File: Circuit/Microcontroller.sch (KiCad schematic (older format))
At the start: 5 parts, among them CON501 AVR-ISP-10, IC501 ATMEGA644-A, Y501 Crystal

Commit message: Additional PCB work
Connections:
- net ADC0: now also IC501.34 ((PCINT3/ADC3)PA3); no longer IC501.37 ((PCINT0/ADC0)PA0)
- net ADC1: now also IC501.35 ((PCINT2/ADC2)PA2); no longer IC501.36 ((PCINT1/ADC1)PA1)
- net ADC2: now also IC501.36 ((PCINT1/ADC1)PA1); no longer IC501.35 ((PCINT2/ADC2)PA2)
- net ADC3: now also IC501.37 ((PCINT0/ADC0)PA0); no longer IC501.34 ((PCINT3/ADC3)PA3)
- net RST: now also IC501.44 ((PCINT12/OC0B/~SS~)PB4)
- net PD1: now reaches IC501.10 ((PCINT25/TXD0)PD1)
- net PD2: now reaches IC501.11 ((PCINT26/INT0)PD2)
- net PD3: now reaches IC501.12 ((PCINT27/INT1)PD3)
- net PD4: now reaches IC501.13 ((PCINT28/OC1B)PD4)
- net PD5: now reaches IC501.14 ((PCINT294/OC1A)PD5)
- net PD6: now reaches IC501.15 ((PCINT30/OC2B/ICP)PD6)
- net PD7: now reaches IC501.16 ((PCINT31/OC2A)PD7)
- net PC0: now reaches IC501.19 ((PCINT16/SCL)PC0)
- net PC1: now reaches IC501.20 ((PCINT17/SDA)PC1)
- net PC2: now reaches IC501.21 ((PCINT18/TCK)PC2)
- net PC3: now reaches IC501.22 ((PCINT19/TMS)PC3)
- net PC4: now reaches IC501.23 ((PCINT20/TDO)PC4)
- net PC5: now reaches IC501.24 ((PCINT21/TDI)PC5)
- net PC6: now reaches IC501.25 ((PCINT22/TOSC1)PC6)
- net PC7: now reaches IC501.26 ((PCINT23/TOSC2)PC7)
- net WR: now reaches IC501.42 ((PCINT10/AIN0/INT2)PB2)
- net CS: now reaches IC501.43 ((PCINT11/AIN1/OC0A)PB3)
- net PD0: now reaches IC501.9 ((PCINT24/RXD0)PD0)
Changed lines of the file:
@@
 $EndComp
 $Comp
-L GND #PWR048
+L GND #PWR503
 U 1 1 58AFDD43
 P 5150 5750
-F 0 "#PWR048" H 5150 5500 50  0001 C CNN
+F 0 "#PWR503" H 5150 5500 50  0001 C CNN
 F 1 "GND" H 5150 5600 50  0000 C CNN
 F 2 "" H 5150 5750 50  0000 C CNN
@@
 $EndComp
 $Comp
-L GND #PWR049
+L GND #PWR504
 U 1 1 58AFDD54
 P 5350 5750
-F 0 "#PWR049" H 5350 5500 50  0001 C CNN
+F 0 "#PWR504" H 5350 5500 50  0001 C CNN
 F 1 "GND" H 5350 5600 50  0000 C CNN
 F 2 "" H 5350 5750 50  0000 C CNN
@@
 $EndComp
 $Comp
-L GND #PWR050
+L GND #PWR506
 U 1 1 58AFDD65
 P 5550 5750
-F 0 "#PWR050" H 5550 5500 50  0001 C CNN
+F 0 "#PWR506" H 5550 5500 50  0001 C CNN
 F 1 "GND" H 5550 5600 50  0000 C CNN
 F 2 "" H 5550 5750 50  0000 C CNN
@@
 $EndComp
 $Comp
-L GND #PWR051
+L GND #PWR507
 U 1 1 58AFDD76
 P 5750 5750
-F 0 "#PWR051" H 5750 5500 50  0001 C CNN
+F 0 "#PWR507" H 5750 5500 50  0001 C CNN
 F 1 "GND" H 5750 5600 50  0000 C CNN
 F 2 "" H 5750 5750 50  0000 C CNN
@@
 	5600 5700 5600 5650
 $Comp
-L +3.3V #PWR052
+L +3.3V #PWR505
 U 1 1 58AFDE0F
 P 5400 1500
-F 0 "#PWR052" H 5400 1350 50  0001 C CNN
+F 0 "#PWR505" H 5400 1350 50  0001 C CNN
 F 1 "+3.3V" H 5400 1640 50  0000 C CNN
 F 2 "" H 5400 1500 50  0000 C CNN
@@
 RST
 $Comp
-L +3.3V #PWR053
+L +3.3V #PWR508
 U 1 1 58AFE137
 P 10800 900
-F 0 "#PWR053" H 10800 750 50  0001 C CNN
+F 0 "#PWR508" H 10800 750 50  0001 C CNN
 F 1 "+3.3V" H 10800 1040 50  0000 C CNN
 F 2 "" H 10800 900 50  0000 C CNN
@@
 	10800 1150 10800 900
 $Comp
-L GND #PWR054
+L GND #PWR509
 U 1 1 58AFE166
 P 10800 1700
-F 0 "#PWR054" H 10800 1450 50  0001 C CNN
+F 0 "#PWR509" H 10800 1450 50  0001 C CNN
 F 1 "GND" H 10800 1550 50  0000 C CNN
 F 2 "" H 10800 1700 50  0000 C CNN
@@
 $EndComp
 $Comp
-L GND #PWR055
+L GND #PWR501
 U 1 1 58AFE6AE
 P 3350 2350
-F 0 "#PWR055" H 3350 2100 50  0001 C CNN
+F 0 "#PWR501" H 3350 2100 50  0001 C CNN
 F 1 "GND" H 3350 2200 50  0000 C CNN
 F 2 "" H 3350 2350 50  0000 C CNN
@@
 $EndComp
 $Comp
-L GND #PWR056
+L GND #PWR502
 U 1 1 58AFE704
 P 3350 2750
-F 0 "#PWR056" H 3350 2500 50  0001 C CNN
+F 0 "#PWR502" H 3350 2500 50  0001 C CNN
 F 1 "GND" H 3350 2600 50  0000 C CNN
 F 2 "" H 3350 2750 50  0000 C CNN
@@
 Text HLabel 7000 3550 2    60   Input ~ 0
 SCK
+Text HLabel 7000 2250 2    60   Input ~ 0
+ADC0
+Text HLabel 7000 2150 2    60   Input ~ 0
+ADC1
+Text HLabel 7000 2050 2    60   Input ~ 0
+ADC2
 Text HLabel 7000 1950 2    60   Input ~ 0
-ADC0
-Text HLabel 7000 2050 2    60   Input ~ 0
-ADC1
-Text HLabel 7000 2150 2    60   Input ~ 0
-ADC2
-Text HLabel 7000 2250 2    60   Input ~ 0
 ADC3
 Wire Wire Line
@@
 Wire Wire Line
 	6600 2250 7000 2250
+Wire Wire Line
+	6600 3250 7000 3250
+Wire Wire Line
+	6600 3150 7000 3150
+Wire Wire Line
+	6600 3050 7000 3050
+Text Label 6750 3250 0    60   ~ 0
+RST
+Text Label 6800 3150 0    60   ~ 0
+CS
+Text Label 6800 3050 0    60   ~ 0
+WR
+Text HLabel 7000 3250 2    60   Input ~ 0
+RST
+Text HLabel 7000 3150 2    60   Input ~ 0
+CS
+Text HLabel 7000 3050 2    60   Input ~ 0
+WR
+Wire Wire Line
+	6600 3750 7000 3750
+Wire Wire Line
+	6600 3850 7000 3850
+Wire Wire Line
+	6600 3950 7000 3950
+Wire Wire Line
+	6600 4050 7000 4050
+Wire Wire Line
+	6600 4150 7000 4150
+Wire Wire Line
+	6600 4250 7000 4250
+Wire Wire Line
+	6600 4350 7000 4350
+Wire Wire Line
+	6600 4450 7000 4450
+Text HLabel 7000 3750 2    60   Input ~ 0
+PC0
+Text HLabel 7000 3850 2    60   Input ~ 0
+PC1
+Text HLabel 7000 3950 2    60   Input ~ 0
+PC2
+Text HLabel 7000 4050 2    60   Input ~ 0
+PC3
+Text HLabel 7000 4150 2    60   Input ~ 0
+PC4
+Text HLabel 7000 4250 2    60   Input ~ 0
+PC5
+Text HLabel 7000 4350 2    60   Input ~ 0
+PC6
+Text HLabel 7000 4450 2    60   Input ~ 0
+PC7
+Wire Wire Line
+	6600 4650 7000 4650
+Wire Wire Line
+	6600 4750 7000 4750
+Wire Wire Line
+	6600 4850 7000 4850
+Wire Wire Line
+	6600 4950 7000 4950
+Wire Wire Line
+	6600 5050 7000 5050
+Wire Wire Line
+	6600 5150 7000 5150
+Wire Wire Line
+	6600 5250 7000 5250
+Wire Wire Line
+	6600 5350 7000 5350
+Text HLabel 7000 4650 2    60   Input ~ 0
+PD0
+Text HLabel 7000 4750 2    60   Input ~ 0
+PD1
+Text HLabel 7000 4850 2    60   Input ~ 0
+PD2
+Text HLabel 7000 4950 2    60   Input ~ 0
+PD3
+Text HLabel 7000 5050 2    60   Input ~ 0
+PD4
+Text HLabel 7000 5150 2    60   Input ~ 0
+PD5
+Text HLabel 7000 5250 2    60   Input ~ 0
+PD6
+Text HLabel 7000 5350 2    60   Input ~ 0
+PD7
 $EndSCHEMATC

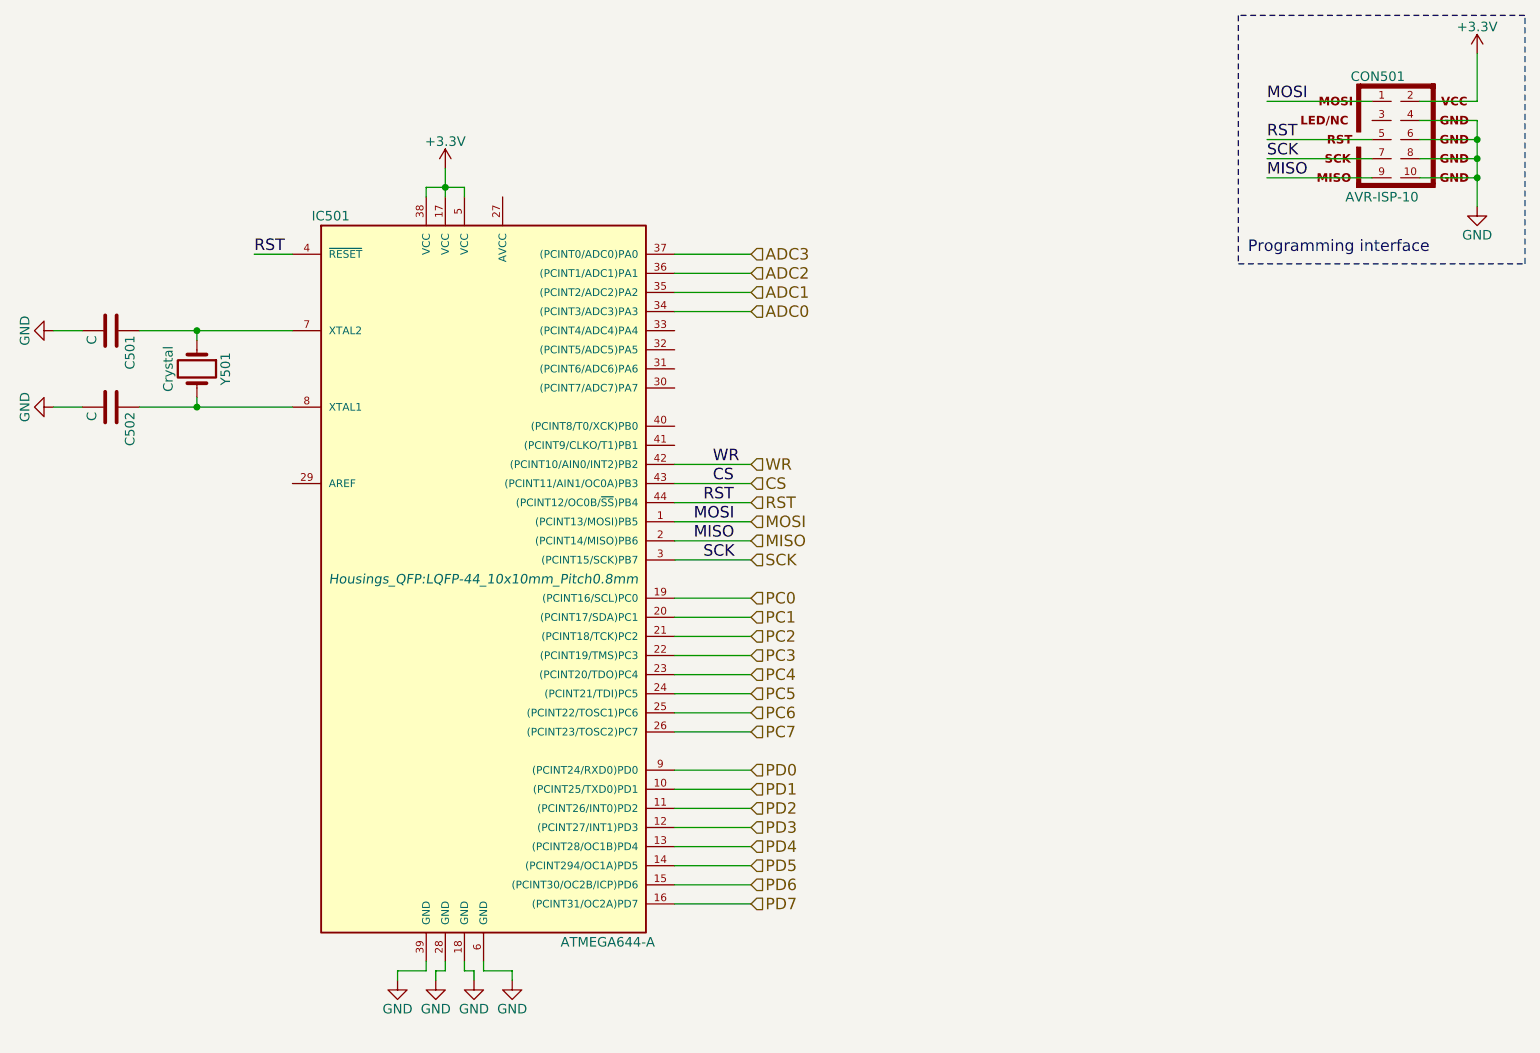
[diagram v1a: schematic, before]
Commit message: Routed PCB and made backup. Footprint for Optocouplers
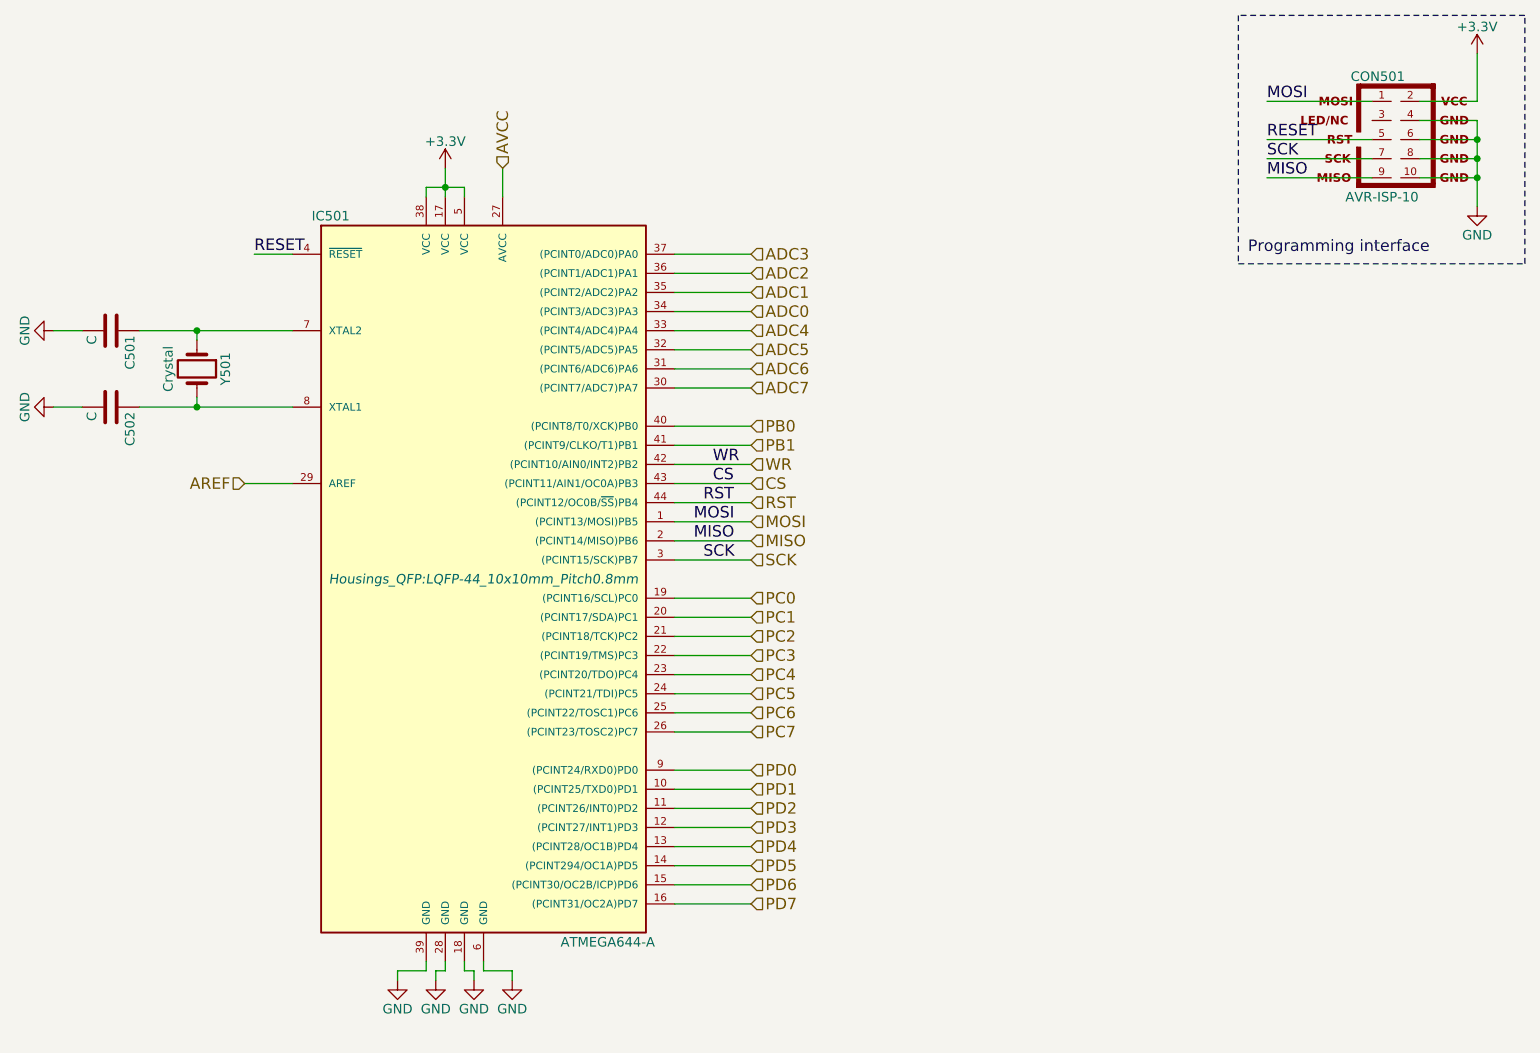
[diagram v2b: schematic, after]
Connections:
- net RST: no longer CON501.5, IC501.4 (~RESET)
- net AVCC: now reaches IC501.27 (AVCC)
- net AREF: now reaches IC501.29 (AREF)
- net ADC7: now reaches IC501.30 ((PCINT7/ADC7)PA7)
- net ADC6: now reaches IC501.31 ((PCINT6/ADC6)PA6)
- net ADC5: now reaches IC501.32 ((PCINT5/ADC5)PA5)
- net ADC4: now reaches IC501.33 ((PCINT4/ADC4)PA4)
- net PB0: now reaches IC501.40 ((PCINT8/T0/XCK)PB0)
- net PB1: now reaches IC501.41 ((PCINT9/CLKO/T1)PB1)
- new net RESET: CON501.5, IC501.4 (~RESET)
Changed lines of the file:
@@
 $EndComp
 $Comp
-L GND #PWR503
+L GND #PWR044
 U 1 1 58AFDD43
 P 5150 5750
-F 0 "#PWR503" H 5150 5500 50  0001 C CNN
+F 0 "#PWR044" H 5150 5500 50  0001 C CNN
 F 1 "GND" H 5150 5600 50  0000 C CNN
 F 2 "" H 5150 5750 50  0000 C CNN
@@
 $EndComp
 $Comp
-L GND #PWR504
+L GND #PWR045
 U 1 1 58AFDD54
 P 5350 5750
-F 0 "#PWR504" H 5350 5500 50  0001 C CNN
+F 0 "#PWR045" H 5350 5500 50  0001 C CNN
 F 1 "GND" H 5350 5600 50  0000 C CNN
 F 2 "" H 5350 5750 50  0000 C CNN
@@
 $EndComp
 $Comp
-L GND #PWR506
+L GND #PWR046
 U 1 1 58AFDD65
 P 5550 5750
-F 0 "#PWR506" H 5550 5500 50  0001 C CNN
+F 0 "#PWR046" H 5550 5500 50  0001 C CNN
 F 1 "GND" H 5550 5600 50  0000 C CNN
 F 2 "" H 5550 5750 50  0000 C CNN
@@
 $EndComp
 $Comp
-L GND #PWR507
+L GND #PWR047
 U 1 1 58AFDD76
 P 5750 5750
-F 0 "#PWR507" H 5750 5500 50  0001 C CNN
+F 0 "#PWR047" H 5750 5500 50  0001 C CNN
 F 1 "GND" H 5750 5600 50  0000 C CNN
 F 2 "" H 5750 5750 50  0000 C CNN
@@
 	5600 5700 5600 5650
 $Comp
-L +3.3V #PWR505
+L +3.3V #PWR048
 U 1 1 58AFDE0F
 P 5400 1500
-F 0 "#PWR505" H 5400 1350 50  0001 C CNN
+F 0 "#PWR048" H 5400 1350 50  0001 C CNN
 F 1 "+3.3V" H 5400 1640 50  0000 C CNN
 F 2 "" H 5400 1500 50  0000 C CNN
@@
 	10250 1350 9700 1350
 Text Label 9700 1350 0    60   ~ 0
-RST
+RESET
 Wire Wire Line
 	4600 1950 4400 1950
 Text Label 4400 1950 0    60   ~ 0
-RST
-$Comp
-L +3.3V #PWR508
+RESET
+$Comp
+L +3.3V #PWR049
 U 1 1 58AFE137
 P 10800 900
-F 0 "#PWR508" H 10800 750 50  0001 C CNN
+F 0 "#PWR049" H 10800 750 50  0001 C CNN
 F 1 "+3.3V" H 10800 1040 50  0000 C CNN
 F 2 "" H 10800 900 50  0000 C CNN
@@
 	10800 1150 10800 900
 $Comp
-L GND #PWR509
+L GND #PWR050
 U 1 1 58AFE166
 P 10800 1700
-F 0 "#PWR509" H 10800 1450 50  0001 C CNN
+F 0 "#PWR050" H 10800 1450 50  0001 C CNN
 F 1 "GND" H 10800 1550 50  0000 C CNN
 F 2 "" H 10800 1700 50  0000 C CNN
@@
 $EndComp
 $Comp
-L GND #PWR501
+L GND #PWR051
 U 1 1 58AFE6AE
 P 3350 2350
-F 0 "#PWR501" H 3350 2100 50  0001 C CNN
+F 0 "#PWR051" H 3350 2100 50  0001 C CNN
 F 1 "GND" H 3350 2200 50  0000 C CNN
 F 2 "" H 3350 2350 50  0000 C CNN
@@
 $EndComp
 $Comp
-L GND #PWR502
+L GND #PWR052
 U 1 1 58AFE704
 P 3350 2750
-F 0 "#PWR502" H 3350 2500 50  0001 C CNN
+F 0 "#PWR052" H 3350 2500 50  0001 C CNN
 F 1 "GND" H 3350 2600 50  0000 C CNN
 F 2 "" H 3350 2750 50  0000 C CNN
@@
 Wire Wire Line
 	6600 3050 7000 3050
-Text Label 6750 3250 0    60   ~ 0
-RST
 Text Label 6800 3150 0    60   ~ 0
 CS
@@
 Text HLabel 7000 5350 2    60   Input ~ 0
 PD7
+Text HLabel 7000 2350 2    60   Input ~ 0
+ADC4
+Text HLabel 7000 2450 2    60   Input ~ 0
+ADC5
+Text HLabel 7000 2550 2    60   Input ~ 0
+ADC6
+Text HLabel 7000 2650 2    60   Input ~ 0
+ADC7
+Wire Wire Line
+	6600 2350 7000 2350
+Wire Wire Line
+	6600 2450 7000 2450
+Wire Wire Line
+	6600 2550 7000 2550
+Wire Wire Line
+	6600 2650 7000 2650
+Text HLabel 7000 2850 2    60   Input ~ 0
+PB0
+Text HLabel 7000 2950 2    60   Input ~ 0
+PB1
+Wire Wire Line
+	6600 2850 7000 2850
+Wire Wire Line
+	6600 2950 7000 2950
+Text HLabel 5700 1500 1    60   Input ~ 0
+AVCC
+Wire Wire Line
+	5700 1500 5700 1650
+Text HLabel 4350 3150 0    60   Input ~ 0
+AREF
+Wire Wire Line
+	4350 3150 4600 3150
+Text Label 6750 3250 0    60   ~ 0
+RST
 $EndSCHEMATC

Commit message: PCB. Pours mostly complete. Almost done?
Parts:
- added C503, C504, C506, C509: 100uF, Capacitors_SMD:C_0805, symbol C
- added L501: 10uH, Capacitors_SMD:C_1206, symbol L
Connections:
- net +3V3: now also C503.2, C504.2, C506.2, L501.1
- net GND: now also C503.1, C504.1, C506.1, C509.1
- net AVCC: no longer names the net of IC501.27 (AVCC)
- net AVCC: now also C509.2, L501.2

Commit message: PCB Revision 1
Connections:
- net PB0 is gone; now on net RST: IC501.40 ((PCINT8/T0/XCK)PB0)
- net PB1 is gone; now on net WR: IC501.41 ((PCINT9/CLKO/T1)PB1)
- net CS: now also IC501.42 ((PCINT10/AIN0/INT2)PB2); no longer IC501.43 ((PCINT11/AIN1/OC0A)PB3)
- net RST: no longer IC501.44 ((PCINT12/OC0B/~SS~)PB4)
- net WR: no longer IC501.42 ((PCINT10/AIN0/INT2)PB2)
- new net PB3: IC501.43 ((PCINT11/AIN1/OC0A)PB3)
- new net PB4: IC501.44 ((PCINT12/OC0B/~SS~)PB4)
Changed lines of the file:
@@
 Wire Wire Line
 	6600 3050 7000 3050
-Text Label 6800 3150 0    60   ~ 0
+Text Label 6800 3050 0    60   ~ 0
 CS
-Text Label 6800 3050 0    60   ~ 0
+Text Label 6800 2950 0    60   ~ 0
 WR
-Text HLabel 7000 3250 2    60   Input ~ 0
+Text HLabel 7000 2850 2    60   Input ~ 0
 RST
-Text HLabel 7000 3150 2    60   Input ~ 0
+Text HLabel 7000 3050 2    60   Input ~ 0
 CS
-Text HLabel 7000 3050 2    60   Input ~ 0
+Text HLabel 7000 2950 2    60   Input ~ 0
 WR
 Wire Wire Line
@@
 Wire Wire Line
 	6600 2650 7000 2650
-Text HLabel 7000 2850 2    60   Input ~ 0
-PB0
-Text HLabel 7000 2950 2    60   Input ~ 0
-PB1
+Text HLabel 7000 3150 2    60   Input ~ 0
+PB3
+Text HLabel 7000 3250 2    60   Input ~ 0
+PB4
 Wire Wire Line
 	6600 2850 7000 2850
@@
 Wire Wire Line
 	4350 3150 4600 3150
-Text Label 6750 3250 0    60   ~ 0
+Text Label 6750 2850 0    60   ~ 0
 RST
 $Comp
@@
 Connection ~ 4700 1400
 $Comp
-L GND #PWR?
+L GND #PWR065
 U 1 1 58B90CAA
 P 5350 5850
-F 0 "#PWR?" H 5350 5600 50  0001 C CNN
+F 0 "#PWR065" H 5350 5600 50  0001 C CNN
 F 1 "GND" H 5350 5700 50  0000 C CNN
 F 2 "" H 5350 5850 50  0000 C CNN
@@
 $EndComp
 $Comp
-L GND #PWR?
+L GND #PWR066
 U 1 1 58B90D02
 P 5550 5850
-F 0 "#PWR?" H 5550 5600 50  0001 C CNN
+F 0 "#PWR066" H 5550 5600 50  0001 C CNN
 F 1 "GND" H 5550 5700 50  0000 C CNN
 F 2 "" H 5550 5850 50  0000 C CNN
@@
 $EndComp
 $Comp
-L GND #PWR?
+L GND #PWR067
 U 1 1 58B90D2B
 P 5750 5850
-F 0 "#PWR?" H 5750 5600 50  0001 C CNN
+F 0 "#PWR067" H 5750 5600 50  0001 C CNN
 F 1 "GND" H 5750 5700 50  0000 C CNN
 F 2 "" H 5750 5850 50  0000 C CNN
@@
 $EndComp
 $Comp
-L GND #PWR?
+L GND #PWR068
 U 1 1 58B90D54
 P 5150 5850
-F 0 "#PWR?" H 5150 5600 50  0001 C CNN
+F 0 "#PWR068" H 5150 5600 50  0001 C CNN
 F 1 "GND" H 5150 5700 50  0000 C CNN
 F 2 "" H 5150 5850 50  0000 C CNN
